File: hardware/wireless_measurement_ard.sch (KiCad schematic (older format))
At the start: 23 parts, among them J1 Conn_01x08, J2 Tag-Connect, SW1 SW_SPDT, U1 EFM8LB1, U2 JDY-08, U3 MCP16415, U4 MAX44284

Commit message: fixed powersupply
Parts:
- added C7: 4.7uF, Capacitor_SMD:C_0603_1608Metric_Pad1.08x0.95mm_HandSolder, symbol Device:C
- U1: symbol MCU_SiliconLabs:EFM8LB1 -> wireless_measurement_ard-rescue:EFM8LB1-MCU_SiliconLabs
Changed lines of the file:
@@
 VIN
 $Comp
-L MCU_SiliconLabs:EFM8LB1 U1
+L wireless_measurement_ard-rescue:EFM8LB1-MCU_SiliconLabs U1
 U 1 1 611E9E7B
 P 5850 2000
@@
 Text GLabel 9300 3300 0    50   Input ~ 0
 A4
+$Comp
+L Device:C C7
+U 1 1 6152B86D
+P 5250 1100
+F 0 "C7" H 5000 1150 50  0000 L CNN
+F 1 "4.7uF" H 4950 1050 50  0000 L CNN
+F 2 "Capacitor_SMD:C_0603_1608Metric_Pad1.08x0.95mm_HandSolder" H 5288 950 50  0001 C CNN
+F 3 "~" H 5250 1100 50  0001 C CNN
+	1    5250 1100
+	1    0    0    -1
+$EndComp
+$Comp
+L power:+3.3V #PWR0102
+U 1 1 6152C109
+P 5250 950
+F 0 "#PWR0102" H 5250 800 50  0001 C CNN
+F 1 "+3.3V" H 5265 1123 50  0000 C CNN
+F 2 "" H 5250 950 50  0001 C CNN
+F 3 "" H 5250 950 50  0001 C CNN
+	1    5250 950
+	1    0    0    -1
+$EndComp
 $EndSCHEMATC

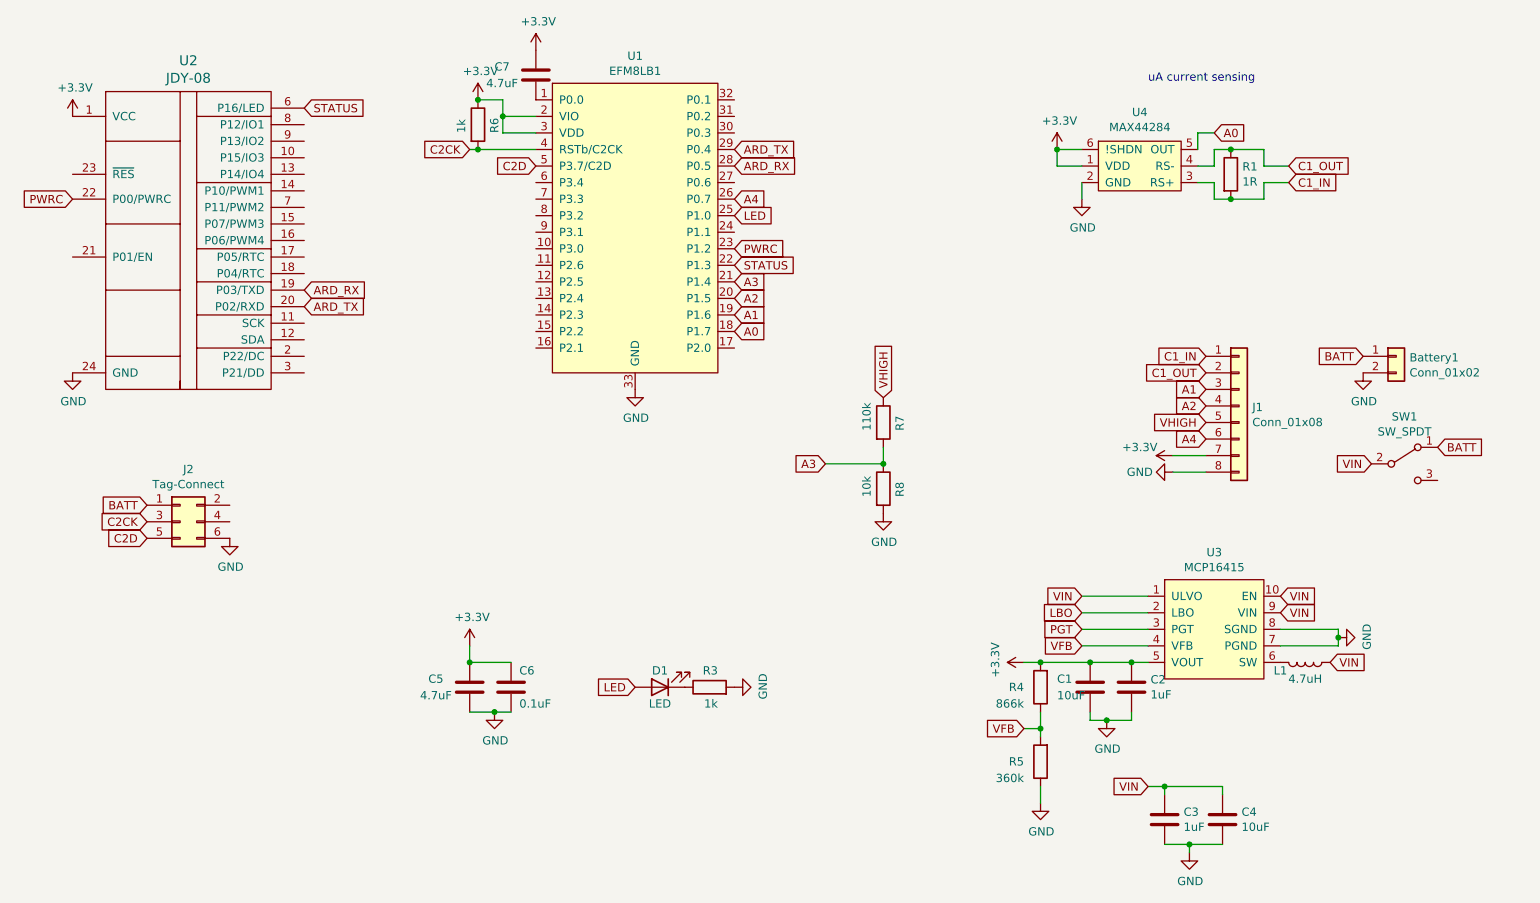
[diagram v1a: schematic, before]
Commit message: added bidrectional current flow
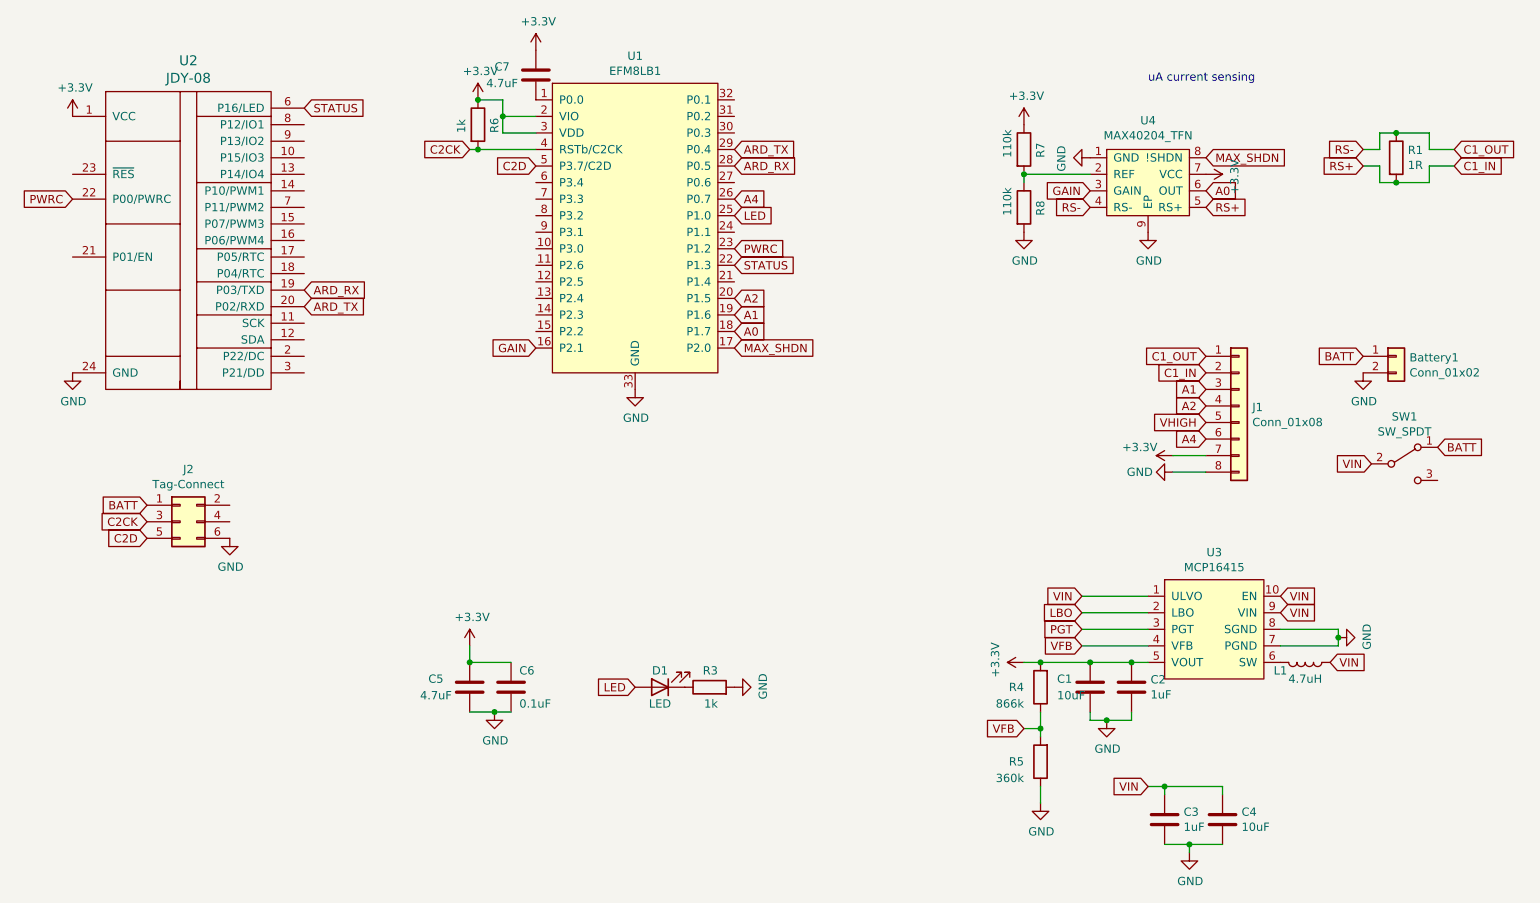
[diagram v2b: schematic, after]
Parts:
- removed U4: MAX44284, Package_TO_SOT_SMD:SOT-23-6_Handsoldering, symbol wireless_measurement_ard-rescue:MAX44284
- added U4: MAX40204_TFN, Package_DFN_QFN:DFN-8-1EP_2x2mm_P0.5mm_EP0.7x1.3mm, symbol ben_common:MAX40204_TFN
- R8: value 10k -> 110k
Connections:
- net +3V3: now also R7.1, U4.7 (VCC)
- net A0: now also U4.6 (OUT)
- net C1_IN: now also J1.2 (Pin_2), U4.5 (RS+); no longer J1.1 (Pin_1)
- net C1_OUT: now also J1.1 (Pin_1), U4.4 (RS-); no longer J1.2 (Pin_2)
- net GND: now also U4.1 (GND), U4.9 (EP)
- net VHIGH: no longer R7.1
- net GAIN: now reaches U1.16 (P2.1)
- net GAIN: now also U4.3 (GAIN)
- net MAX_SHDN: now reaches U1.17 (P2.0)
- net MAX_SHDN: now also U4.8 (!SHDN)
- net A3: no longer names the net of R7.2, R8.1
- net A3: now also U4.2 (REF); no longer U1.21 (P1.4)
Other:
- moved on the sheet: R1, R7, R8
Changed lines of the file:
@@
 	1    0    0    -1
 $EndComp
-$Comp
-L power:GND #PWR0101
-U 1 1 60F7603A
-P 8550 1850
-F 0 "#PWR0101" H 8550 1600 50  0001 C CNN
-F 1 "GND" H 8555 1677 50  0000 C CNN
-F 2 "" H 8550 1850 50  0001 C CNN
-F 3 "" H 8550 1850 50  0001 C CNN
-	1    8550 1850
-	1    0    0    -1
-$EndComp
-Wire Wire Line
-	8550 1650 8400 1650
-Text GLabel 9350 1450 2    50   Input ~ 0
-A0
 Text GLabel 9300 3000 0    50   Input ~ 0
 A1
 Wire Wire Line
-	9250 1650 9350 1650
-Wire Wire Line
-	9350 1650 9350 1550
-Wire Wire Line
-	9250 1750 9350 1750
-Wire Wire Line
-	9350 1750 9350 1850
-Connection ~ 9450 1550
-Connection ~ 9450 1850
-Wire Wire Line
-	9450 1850 9650 1850
-Wire Wire Line
-	9350 1850 9450 1850
-Wire Wire Line
-	9450 1550 9650 1550
-Wire Wire Line
-	9350 1550 9450 1550
+	10250 1550 10350 1550
+Wire Wire Line
+	10350 1550 10350 1450
+Wire Wire Line
+	10250 1650 10350 1650
+Wire Wire Line
+	10350 1650 10350 1750
+Connection ~ 10450 1450
+Connection ~ 10450 1750
+Wire Wire Line
+	10450 1750 10650 1750
+Wire Wire Line
+	10350 1750 10450 1750
+Wire Wire Line
+	10450 1450 10650 1450
+Wire Wire Line
+	10350 1450 10450 1450
 $Comp
 L Device:R R1
 U 1 1 60F77736
-P 9450 1700
-F 0 "R1" H 9520 1746 50  0000 L CNN
-F 1 "1R" H 9520 1655 50  0000 L CNN
-F 2 "Resistor_SMD:R_0805_2012Metric_Pad1.15x1.40mm_HandSolder" V 9380 1700 50  0001 C CNN
-F 3 "~" H 9450 1700 50  0001 C CNN
-	1    9450 1700
-	1    0    0    -1
-$EndComp
-Wire Wire Line
-	9650 1850 9650 1750
-Wire Wire Line
-	9650 1650 9650 1550
+P 10450 1600
+F 0 "R1" H 10520 1646 50  0000 L CNN
+F 1 "1R" H 10520 1555 50  0000 L CNN
+F 2 "Resistor_SMD:R_0805_2012Metric_Pad1.15x1.40mm_HandSolder" V 10380 1600 50  0001 C CNN
+F 3 "~" H 10450 1600 50  0001 C CNN
+	1    10450 1600
+	1    0    0    -1
+$EndComp
+Wire Wire Line
+	10650 1750 10650 1650
+Wire Wire Line
+	10650 1550 10650 1450
 Text Notes 8950 1150 0    50   ~ 0
 uA current sensing
@@
 	0    1    1    0
 $EndComp
-Text GLabel 9800 1750 2    50   Input ~ 0
+Text GLabel 10800 1650 2    50   Input ~ 0
 C1_IN
 Wire Wire Line
-	9650 1750 9800 1750
-Wire Wire Line
-	9650 1650 9800 1650
+	10650 1650 10800 1650
+Wire Wire Line
+	10650 1550 10800 1550
+Text GLabel 9300 2900 0    50   Input ~ 0
+C1_IN
+Text GLabel 10800 1550 2    50   Input ~ 0
+C1_OUT
 Text GLabel 9300 2800 0    50   Input ~ 0
-C1_IN
-Text GLabel 9800 1650 2    50   Input ~ 0
-C1_OUT
-Text GLabel 9300 2900 0    50   Input ~ 0
 C1_OUT
 Text GLabel 8550 4250 0    50   Input ~ 0
@@
 	1    0    0    -1
 $EndComp
-Wire Wire Line
-	8550 1750 8550 1850
 $Comp
 L power:+3.3V #PWR0118
@@
 Text GLabel 6450 2250 2    50   Input ~ 0
 STATUS
-Text GLabel 6450 2350 2    50   Input ~ 0
-A3
+Text GLabel 5250 2750 0    50   Input ~ 0
+GAIN
 Text GLabel 6450 2450 2    50   Input ~ 0
 A2
-Text GLabel 6450 2550 2    50   Input ~ 0
-A1
 $Comp
 L power:GND #PWR0104
@@
 Text GLabel 6450 1950 2    50   Input ~ 0
 LED
-Text GLabel 6450 2650 2    50   Input ~ 0
-A0
 $Comp
 L Connector_Generic:Conn_02x03_Odd_Even J2
@@
 L Device:R R7
 U 1 1 6131256B
-P 7350 3200
-F 0 "R7" V 7450 3150 50  0000 L CNN
-F 1 "110k" V 7250 3150 50  0000 L CNN
-F 2 "Resistor_SMD:R_0603_1608Metric_Pad0.98x0.95mm_HandSolder" V 7280 3200 50  0001 C CNN
-F 3 "~" H 7350 3200 50  0001 C CNN
-	1    7350 3200
+P 8200 1550
+F 0 "R7" V 8300 1500 50  0000 L CNN
+F 1 "110k" V 8100 1500 50  0000 L CNN
+F 2 "Resistor_SMD:R_0603_1608Metric_Pad0.98x0.95mm_HandSolder" V 8130 1550 50  0001 C CNN
+F 3 "~" H 8200 1550 50  0001 C CNN
+	1    8200 1550
 	1    0    0    -1
 $EndComp
@@
 L Device:R R8
 U 1 1 61316095
-P 7350 3600
-F 0 "R8" V 7450 3550 50  0000 L CNN
-F 1 "10k" V 7250 3550 50  0000 L CNN
-F 2 "Resistor_SMD:R_0603_1608Metric_Pad0.98x0.95mm_HandSolder" V 7280 3600 50  0001 C CNN
-F 3 "~" H 7350 3600 50  0001 C CNN
-	1    7350 3600
-	1    0    0    -1
-$EndComp
-$Comp
-L power:GND #PWR0110
-U 1 1 613169FE
-P 7350 3750
-F 0 "#PWR0110" H 7350 3500 50  0001 C CNN
-F 1 "GND" H 7355 3577 50  0000 C CNN
-F 2 "" H 7350 3750 50  0001 C CNN
-F 3 "" H 7350 3750 50  0001 C CNN
-	1    7350 3750
-	1    0    0    -1
-$EndComp
-Text GLabel 7350 3050 1    50   Input ~ 0
-VHIGH
-Wire Wire Line
-	7350 3350 7350 3450
-Text GLabel 7000 3450 0    50   Input ~ 0
-A3
-Wire Wire Line
-	7350 3450 7000 3450
-Connection ~ 7350 3450
-$Comp
-L wireless_measurement_ard-rescue:MAX44284 U4
-U 1 1 612DBC77
-P 8900 1650
-F 0 "U4" H 8900 1975 50  0000 C CNN
-F 1 "MAX44284" H 8900 1884 50  0000 C CNN
-F 2 "Package_TO_SOT_SMD:SOT-23-6_Handsoldering" H 8900 1450 50  0001 C CNN
-F 3 "https://datasheets.maximintegrated.com/en/ds/MAX44284.pdf" H 8900 1450 50  0001 C CNN
-	1    8900 1650
-	1    0    0    -1
-$EndComp
-Wire Wire Line
-	9250 1550 9250 1450
-Wire Wire Line
-	9250 1450 9350 1450
-Wire Wire Line
-	8550 1550 8400 1550
-Wire Wire Line
-	8400 1550 8400 1650
-$Comp
-L power:+3.3V #PWR0111
-U 1 1 612E1F0B
-P 8400 1550
-F 0 "#PWR0111" H 8400 1400 50  0001 C CNN
-F 1 "+3.3V" H 8415 1723 50  0000 C CNN
-F 2 "" H 8400 1550 50  0001 C CNN
-F 3 "" H 8400 1550 50  0001 C CNN
-	1    8400 1550
-	1    0    0    -1
-$EndComp
-Connection ~ 8400 1550
+P 8200 1900
+F 0 "R8" V 8300 1850 50  0000 L CNN
+F 1 "110k" V 8100 1850 50  0000 L CNN
+F 2 "Resistor_SMD:R_0603_1608Metric_Pad0.98x0.95mm_HandSolder" V 8130 1900 50  0001 C CNN
+F 3 "~" H 8200 1900 50  0001 C CNN
+	1    8200 1900
+	1    0    0    -1
+$EndComp
+Text GLabel 9300 1600 2    50   Input ~ 0
+MAX_SHDN
 Text GLabel 6450 1850 2    50   Input ~ 0
 A4
@@
 	1    0    0    -1
 $EndComp
+$Comp
+L ben_common:MAX40204_TFN U4
+U 1 1 615A0F44
+P 8950 1750
+F 0 "U4" H 8950 2125 50  0000 C CNN
+F 1 "MAX40204_TFN" H 8950 2034 50  0000 C CNN
+F 2 "Package_DFN_QFN:DFN-8-1EP_2x2mm_P0.5mm_EP0.7x1.3mm" H 8850 1450 50  0001 C CNN
+F 3 "" H 8950 1750 50  0001 C CNN
+	1    8950 1750
+	1    0    0    -1
+$EndComp
+$Comp
+L power:GND #PWR0101
+U 1 1 615A1F4D
+P 8950 2050
+F 0 "#PWR0101" H 8950 1800 50  0001 C CNN
+F 1 "GND" H 8955 1877 50  0000 C CNN
+F 2 "" H 8950 2050 50  0001 C CNN
+F 3 "" H 8950 2050 50  0001 C CNN
+	1    8950 2050
+	1    0    0    -1
+$EndComp
+$Comp
+L power:GND #PWR0110
+U 1 1 615A23E8
+P 8600 1600
+F 0 "#PWR0110" H 8600 1350 50  0001 C CNN
+F 1 "GND" H 8605 1427 50  0000 C CNN
+F 2 "" H 8600 1600 50  0001 C CNN
+F 3 "" H 8600 1600 50  0001 C CNN
+	1    8600 1600
+	0    1    1    0
+$EndComp
+$Comp
+L power:+3.3V #PWR0111
+U 1 1 615A4E84
+P 8200 1400
+F 0 "#PWR0111" H 8200 1250 50  0001 C CNN
+F 1 "+3.3V" H 8215 1573 50  0000 C CNN
+F 2 "" H 8200 1400 50  0001 C CNN
+F 3 "" H 8200 1400 50  0001 C CNN
+	1    8200 1400
+	1    0    0    -1
+$EndComp
+$Comp
+L power:GND #PWR0120
+U 1 1 615A53CD
+P 8200 2050
+F 0 "#PWR0120" H 8200 1800 50  0001 C CNN
+F 1 "GND" H 8205 1877 50  0000 C CNN
+F 2 "" H 8200 2050 50  0001 C CNN
+F 3 "" H 8200 2050 50  0001 C CNN
+	1    8200 2050
+	1    0    0    -1
+$EndComp
+$Comp
+L power:+3.3V #PWR0122
+U 1 1 615A8A4D
+P 9300 1700
+F 0 "#PWR0122" H 9300 1550 50  0001 C CNN
+F 1 "+3.3V" H 9315 1873 50  0000 C CNN
+F 2 "" H 9300 1700 50  0001 C CNN
+F 3 "" H 9300 1700 50  0001 C CNN
+	1    9300 1700
+	0    1    1    0
+$EndComp
+Text GLabel 9300 1900 2    50   Input ~ 0
+RS+
+Text GLabel 8600 1900 0    50   Input ~ 0
+RS-
+Wire Wire Line
+	8200 1750 8200 1700
+Wire Wire Line
+	8200 1700 8600 1700
+Connection ~ 8200 1700
+Text GLabel 10250 1650 0    50   Input ~ 0
+RS+
+Text GLabel 10250 1550 0    50   Input ~ 0
+RS-
+Text GLabel 8600 1800 0    50   Input ~ 0
+GAIN
+Text GLabel 9300 1800 2    50   Input ~ 0
+A0
+Text GLabel 6450 2550 2    50   Input ~ 0
+A1
+Text GLabel 6450 2750 2    50   Input ~ 0
+MAX_SHDN
+Text GLabel 6450 2650 2    50   Input ~ 0
+A0
 $EndSCHEMATC
